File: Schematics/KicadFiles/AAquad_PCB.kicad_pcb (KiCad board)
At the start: 2 copper layers, 55.6 x 48.8 mm, 38 parts, among them IC1 L3GD20H, J1 programmer, Q1 BSS138, Q2 BSS138, U1 ATMEGA328-AU, U2 LIS3DHTR

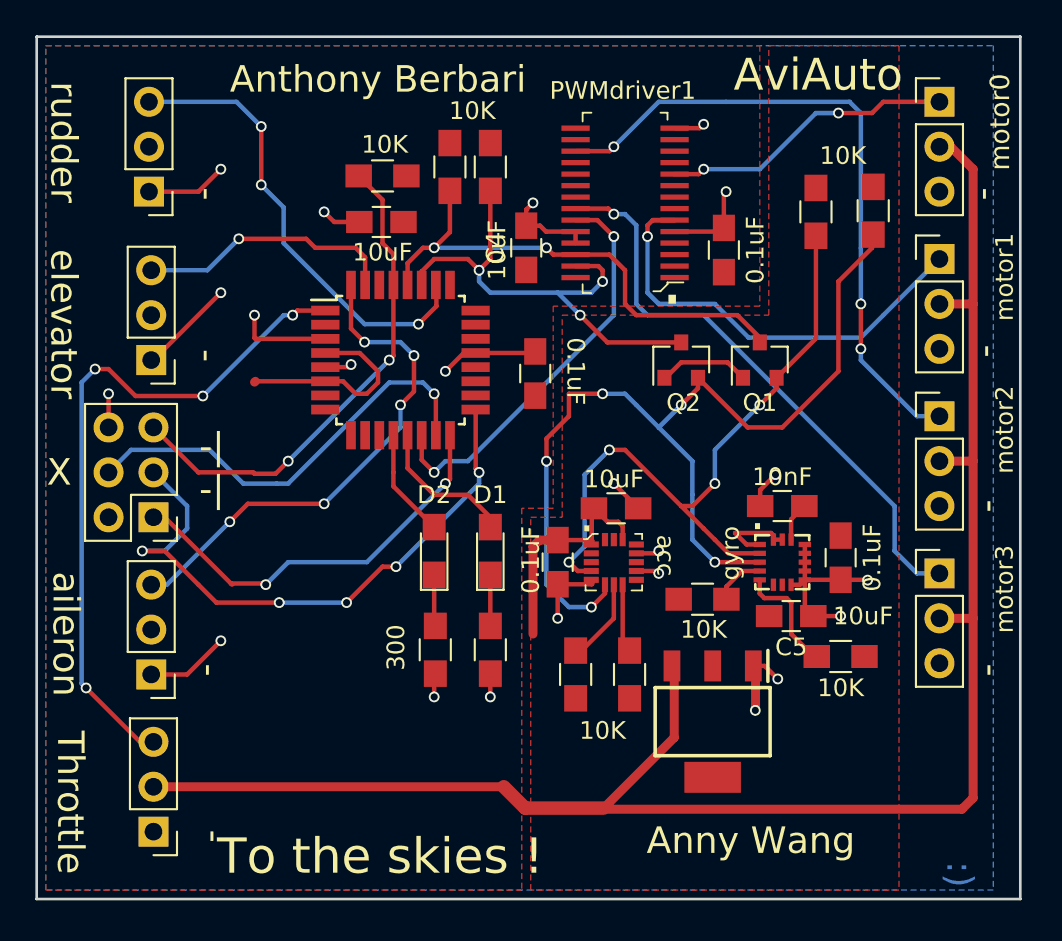
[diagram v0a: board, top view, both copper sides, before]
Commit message: PCB redesign to include IMU, barometer, and various other features
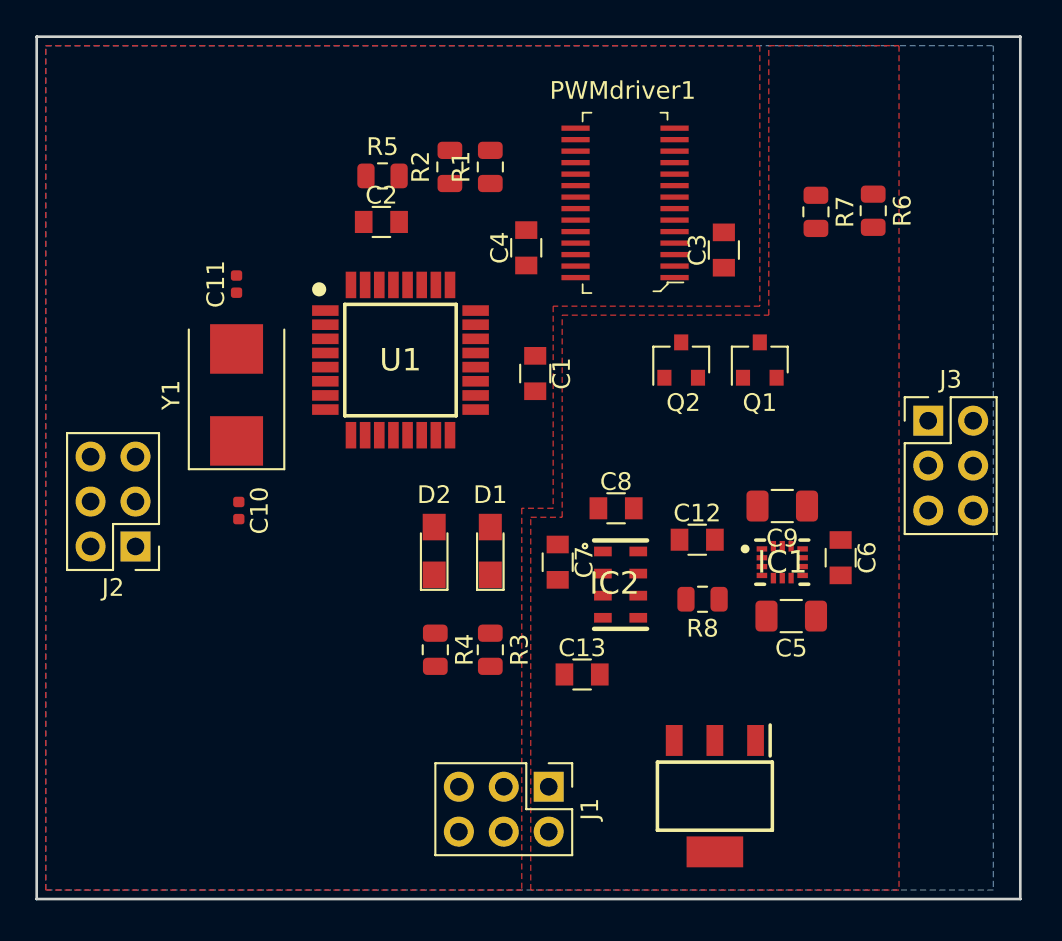
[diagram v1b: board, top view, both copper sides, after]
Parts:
- removed R10, R11, R9: 10K, Resistors_SMD:R_0805_HandSoldering
- removed U2: LIS3DHTR, footprints:Lis3dh
- removed aileron1, elevator1, motor1, motor2, motor3, motor4, rudder1, throttle1: Conn_01x03, Pin_Headers:Pin_Header_Straight_1x03_Pitch2.54mm
- added C10: 33pF, Capacitor_SMD:C_0402_1005Metric, F.Cu at (220.7, 77.1)
- added C11: 33pF, Capacitor_SMD:C_0402_1005Metric, F.Cu at (220.6, 64.3)
- added C12: 0.1uF, Capacitors_SMD:C_0805, F.Cu at (246.7, 78.7)
- added C13: 0.1uF, Capacitors_SMD:C_0805, F.Cu at (240.1, 86.4)
- added IC2: MPL3115A2, sensors:MPL3115A2, F.Cu at (242.3, 81.3)
- added J2: Receiver_Output, Connector_PinHeader_2.54mm:PinHeader_2x03_P2.54mm_Vertical, F.Cu at (214.9, 79.1)
- added J3: ESC_Input, Connector_PinHeader_2.54mm:PinHeader_2x03_P2.54mm_Vertical, F.Cu at (259.7, 72.0)
- added Y1: Crystal, Crystals:Crystal_SMD_7050-2pin_7.0x5.0mm, F.Cu at (220.6, 70.6)
- C1, C2, C3, C4, C6, C7, C8: footprint Capacitors_SMD:C_0805_HandSoldering -> Capacitors_SMD:C_0805
- C5: value 10u -> 100uF; footprint Capacitors_SMD:C_0805_HandSoldering -> Capacitor_SMD:C_1206_3216Metric
- C9: value 10nF -> 100uF; footprint Capacitors_SMD:C_0805_HandSoldering -> Capacitor_SMD:C_1206_3216Metric
- IC1: value L3GD20H -> BMX160; footprint footprints:L3gd20h -> sensors:bmx160
- J1: footprint Pin_Headers:Pin_Header_Straight_2x03_Pitch2.54mm -> Connector_PinHeader_2.54mm:PinHeader_2x03_P2.54mm_Vertical
- R1, R3, R4, R5, R6, R7: footprint Resistors_SMD:R_0805_HandSoldering -> Resistor_SMD:R_0805_2012Metric
- R2, R8: value 10K -> 2K; footprint Resistors_SMD:R_0805_HandSoldering -> Resistor_SMD:R_0805_2012Metric
- U1: value ATMEGA328-AU -> Atmega328pb; footprint Housings_QFP:TQFP-32_7x7mm_Pitch0.8mm -> microcontrollers:ATMEGA328PB-ANR
- moved J1 27.1 mm to (238.3, 92.7), turned to 270 degrees
- moved PS1 4.22 mm to (247.7, 93.2)
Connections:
- net Net-(D1-Pad2) renamed /Led_G
- net Net-(D2-Pad2) renamed /Led_R
- net Net-(J1-Pad1) renamed /MISO_ISP
- net Net-(J1-Pad3) renamed /SWCLK
- net Net-(J1-Pad4) renamed /MOSI_ISP
- net Net-(J1-Pad5) renamed /MCU_RESET
- C1 pad 1: GND -> VCC
- C1 pad 2: VCC -> GND
- C2 pad 1: GND -> VCC
- C2 pad 2: VCC -> GND
- C5 pad 1: GND -> VCC
- C5 pad 2: VAA -> GND
- C6 pad 1: VAA -> GND
- C6 pad 2: GND -> VAA
- C9 pad 1: Net-(C9-Pad1) -> GND
- C9 pad 2: GND -> VAA
- IC1 pad 1: VAA -> /MISO
- IC1 pad 10: GND -> (no net)
- IC1 pad 11: GND -> (no net)
- IC1 pad 12: GND -> /SS_IMU
- IC1 pad 13: GND -> /SCK
- IC1 pad 14: Net-(C9-Pad1) -> /MOSI
- IC1 pad 2: Net-(IC1-Pad2) -> GND
- IC1 pad 3: Net-(IC1-Pad3) -> GND
- IC1 pad 5: Net-(IC1-Pad5) -> VAA
- IC1 pad 6: (no net) -> GND
- IC1 pad 7: (no net) -> GND
- IC1 pad 8: GND -> VAA
- IC1 pad 9: GND -> (no net)
- PWMdriver1 pad 10: Net-(PWMdriver1-Pad10) -> /Motor_2
- PWMdriver1 pad 17: Net-(PWMdriver1-Pad17) -> /Motor_3
- PWMdriver1 pad 22: Net-(PWMdriver1-Pad22) -> /Motor_4
- PWMdriver1 pad 23: Net-(PWMdriver1-Pad23) -> /PWM_OE
- PWMdriver1 pad 26: Net-(PWMdriver1-Pad26) -> /SCL_0
- PWMdriver1 pad 27: Net-(PWMdriver1-Pad27) -> /SDA_0
- PWMdriver1 pad 6: Net-(PWMdriver1-Pad6) -> /Motor_1
- Q1 pad 2: Net-(IC1-Pad2) -> /SDA_1_3.3
- Q1 pad 3: Net-(PWMdriver1-Pad26) -> /SDA_1
- Q2 pad 2: Net-(IC1-Pad3) -> /SCL_1_3.3
- Q2 pad 3: Net-(PWMdriver1-Pad27) -> /SCL_1
- R1 pad 1: Net-(PWMdriver1-Pad27) -> VCC
- R1 pad 2: VCC -> /PWM_OE
- R2 pad 1: Net-(PWMdriver1-Pad26) -> /SCL_0
- R6 pad 2: Net-(IC1-Pad3) -> /SCL_1_3.3
- R7 pad 2: Net-(IC1-Pad2) -> /SDA_1_3.3
- R8 pad 1: Net-(IC1-Pad4) -> /SDA_0
- R8 pad 2: VAA -> VCC
- U1 pad 1: Net-(U1-Pad1) -> /Throttle
- U1 pad 14: Net-(PWMdriver1-Pad23) -> /PWM_OE
- U1 pad 19: (no net) -> /SS_IMU
- U1 pad 22: (no net) -> /MOSI
- U1 pad 23: (no net) -> /MISO
- U1 pad 24: (no net) -> /SCK
- U1 pad 26: Net-(U1-Pad26) -> /Rudder
- U1 pad 27: Net-(PWMdriver1-Pad27) -> /SDA_0
- U1 pad 28: Net-(PWMdriver1-Pad26) -> /SCL_0
- U1 pad 3: GND -> /SDA_1
- U1 pad 31: Net-(U1-Pad31) -> /Elevator
- U1 pad 32: Net-(U1-Pad32) -> /Aileron
- U1 pad 6: VCC -> /SCL_1
- U1 pad 7: (no net) -> /Xtal1
- U1 pad 8: (no net) -> /Xtal2
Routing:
- net VCC: track 112.6 -> 0.00 mm
- net GND: track 71.3 -> 0.00 mm, vias 22 -> 0
- net Net-(IC1-Pad3): track 55.9 -> 0.00 mm, vias 5 -> 0
- net Net-(U1-Pad1): track 39.8 -> 0.00 mm, vias 4 -> 0
- net Net-(IC1-Pad2): track 38.5 -> 0.00 mm, vias 4 -> 0
- net Net-(PWMdriver1-Pad17): track 37.3 -> 0.00 mm, vias 3 -> 0
- net /SWCLK: track 34.5 -> 0.00 mm, vias 5 -> 0
- net Net-(PWMdriver1-Pad22): track 33.2 -> 0.00 mm, vias 1 -> 0
- net Net-(PWMdriver1-Pad27): track 28.8 -> 0.00 mm, vias 3 -> 0
- net Net-(U1-Pad32): track 28.7 -> 0.00 mm, vias 5 -> 0
- net /MCU_RESET: track 28.4 -> 0.00 mm, vias 2 -> 0
- net Net-(PWMdriver1-Pad26): track 28.3 -> 0.00 mm, vias 2 -> 0
- net Net-(PWMdriver1-Pad6): track 26.1 -> 0.00 mm, vias 1 -> 0
- net Net-(U1-Pad26): track 26.0 -> 0.00 mm, vias 3 -> 0
- net /MOSI_ISP: track 25.4 -> 0.00 mm, vias 1 -> 0
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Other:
- board text removed: "-"
- board text removed: "-| -|"
- board text removed: "."
- board text removed: "0.1uF"
- board text removed: "10K"
- board text removed: "10nF"
- board text removed: "10uF"
- board text removed: "300"
- board text removed: ":)"
- board text removed: "Anny Wang"
- board text removed: "Anthony Berbari"
- board text removed: "AviAuto"
- board text removed: "Throttle"
- board text removed: "To the skies !"
- board text removed: "X"
- board text removed: "acc"
- board text removed: "aileron"
- board text removed: "elevator"
- board text removed: "gyro"
- board text removed: "motor0"
- board text removed: "motor1"
- board text removed: "motor2"
- board text removed: "motor3"
- board text removed: "rudder"

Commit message: Completed PCB redesign
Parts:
- removed PWMdriver1: PCA9685PW_112, digikey-footprints:TSSOP-28_W4.40mm
- added C14: 10uF, Capacitor_SMD:C_0805_2012Metric, B.Cu at (236.9, 78.7)
- added C15: 10uF, Capacitor_SMD:C_0805_2012Metric, B.Cu at (236.8, 81.8)
- added C16: 10uF, Capacitor_SMD:C_0805_2012Metric, B.Cu at (236.7, 85.0)
- added C17: 10uF, Capacitor_SMD:C_0805_2012Metric, B.Cu at (236.8, 88.1)
- added IC3: levelShifter, levelShifters:74LVC1T45GW_125, F.Cu at (236.9, 81.8)
- added IC4: levelShifter, levelShifters:74LVC1T45GW_125, F.Cu at (236.8, 84.9)
- added IC5: levelShifter, levelShifters:74LVC1T45GW_125, F.Cu at (236.8, 88.1)
- added IC6: levelShifter, levelShifters:74LVC1T45GW_125, F.Cu at (236.9, 78.6)
- added J4: ultrasonic, Connector_PinHeader_2.54mm:PinHeader_2x02_P2.54mm_Vertical, F.Cu at (235.7, 94.2)
- added REF**: MountingHole_2.5mm_Pad_Via, MountingHole:MountingHole_2.5mm_Pad_Via, F.Cu at (213.1, 53.8)
- added REF**: MountingHole_2.5mm_Pad_Via, MountingHole:MountingHole_2.5mm_Pad_Via, F.Cu at (261.1, 53.8)
- added REF**: MountingHole_2.5mm_Pad_Via, MountingHole:MountingHole_2.5mm_Pad_Via, F.Cu at (261.1, 95.5)
- added REF**: MountingHole_2.5mm_Pad_Via, MountingHole:MountingHole_2.5mm_Pad_Via, F.Cu at (213.1, 95.5)
- added U2: PCA9685PW_112, digikey-footprints:TSSOP-28_W4.40mm, F.Cu at (242.6, 59.7)
- C1, C13, C2, C3, C4, C7, C8: moved to B.Cu
- moved C5 42.0 mm to (213.0, 67.6), turned to 0 degrees
- moved J1 41.1 mm to (221.7, 55.1), turned to 90 degrees
- moved R8 28.9 mm to (228.7, 59.7), turned to 90 degrees
- moved C11 24.3 mm to (215.8, 88.1), turned to 270 degrees
- moved R6 16.0 mm to (244.2, 70.2)
- moved C9 14.9 mm to (254.3, 91.4), turned to 90 degrees
- moved Y1 12.7 mm to (218.4, 83.1), turned to 180 degrees
- moved C2 11.5 mm to (221.0, 69.3), turned to 270 degrees
- moved C10 11.1 mm to (221.0, 88.1)
- moved R7 10.4 mm to (250.6, 70.2)
- moved C13 9.51 mm to (245.8, 78.7)
- moved C7 8.70 mm to (246.5, 76.0), turned to 180 degrees
- moved C12 8.42 mm to (245.9, 87.1), turned to 180 degrees
- moved C1 8.21 mm to (229.4, 70.5), turned to 90 degrees
- moved C3 7.88 mm to (240.9, 65.5), turned to 270 degrees
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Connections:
- IC1 pad 1: /MISO -> /MISO_3.3
- IC1 pad 12: /SS_IMU -> /SS_IMU_3.3
- IC1 pad 13: /SCK -> /SCK_3.3
- IC1 pad 14: /MOSI -> /MOSI_3.3
- IC1 pad 4: Net-(IC1-Pad4) -> (no net)
- J2 pad 4: /Rudder -> /Aileron
- J2 pad 6: /Aileron -> /Rudder
- J3 pad 3: /Motor_1 -> /Motor_3
- J3 pad 4: /Motor_2 -> /Motor_4
- J3 pad 5: /Motor_3 -> /Motor_2
- J3 pad 6: /Motor_4 -> /Motor_1
- U1 pad 10: (no net) -> /Led_G
- U1 pad 12: /Led_R -> /Ultrasonic_Trig
- U1 pad 13: /Led_G -> /Ultrasonic_Echo
- U1 pad 14: /PWM_OE -> (no net)
- U1 pad 25: (no net) -> /PWM_OE
- U1 pad 9: (no net) -> /Led_R
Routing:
- net GND: track 0.00 -> 42.4 mm, vias 0 -> 25
- net /Ultrasonic_Echo: track 0.00 -> 31.8 mm, vias 0 -> 1
- net /Motor_1: track 0.00 -> 31.0 mm
- net VCC: track 0.00 -> 30.7 mm, vias 0 -> 8
- net /Ultrasonic_Trig: track 0.00 -> 30.1 mm, vias 0 -> 1
- net /SDA_1: track 0.00 -> 29.7 mm, vias 0 -> 2
- net /MOSI_ISP: track 0.00 -> 28.7 mm, vias 0 -> 1
- net /Rudder: track 0.00 -> 27.6 mm, vias 0 -> 2
- net /MISO: track 0.00 -> 27.1 mm, vias 0 -> 4
- net /Motor_4: track 0.00 -> 26.4 mm
- net /Motor_2: track 0.00 -> 24.5 mm
- net /Motor_3: track 0.00 -> 24.3 mm
- net /MISO_ISP: track 0.00 -> 22.8 mm, vias 0 -> 1
- net /MOSI: track 0.00 -> 22.6 mm, vias 0 -> 3
- net /SWCLK: track 0.00 -> 22.4 mm, vias 0 -> 1
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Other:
- board text added: ":)"
- board text added: "AAQuad 3.0"
- board text added: "Anny Wang"
- board text added: "Anthony Berbari"
- board text added: "To Freedom !"
- board text added: "To the skies!"
